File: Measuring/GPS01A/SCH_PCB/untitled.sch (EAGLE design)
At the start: 38 parts, among them SW1 1.55V, T5 BC817, U1 LE33CD-TR, X2 SROUB3M, X3 SROUB3M, X4 SROUB3M, X5 SROUB3M

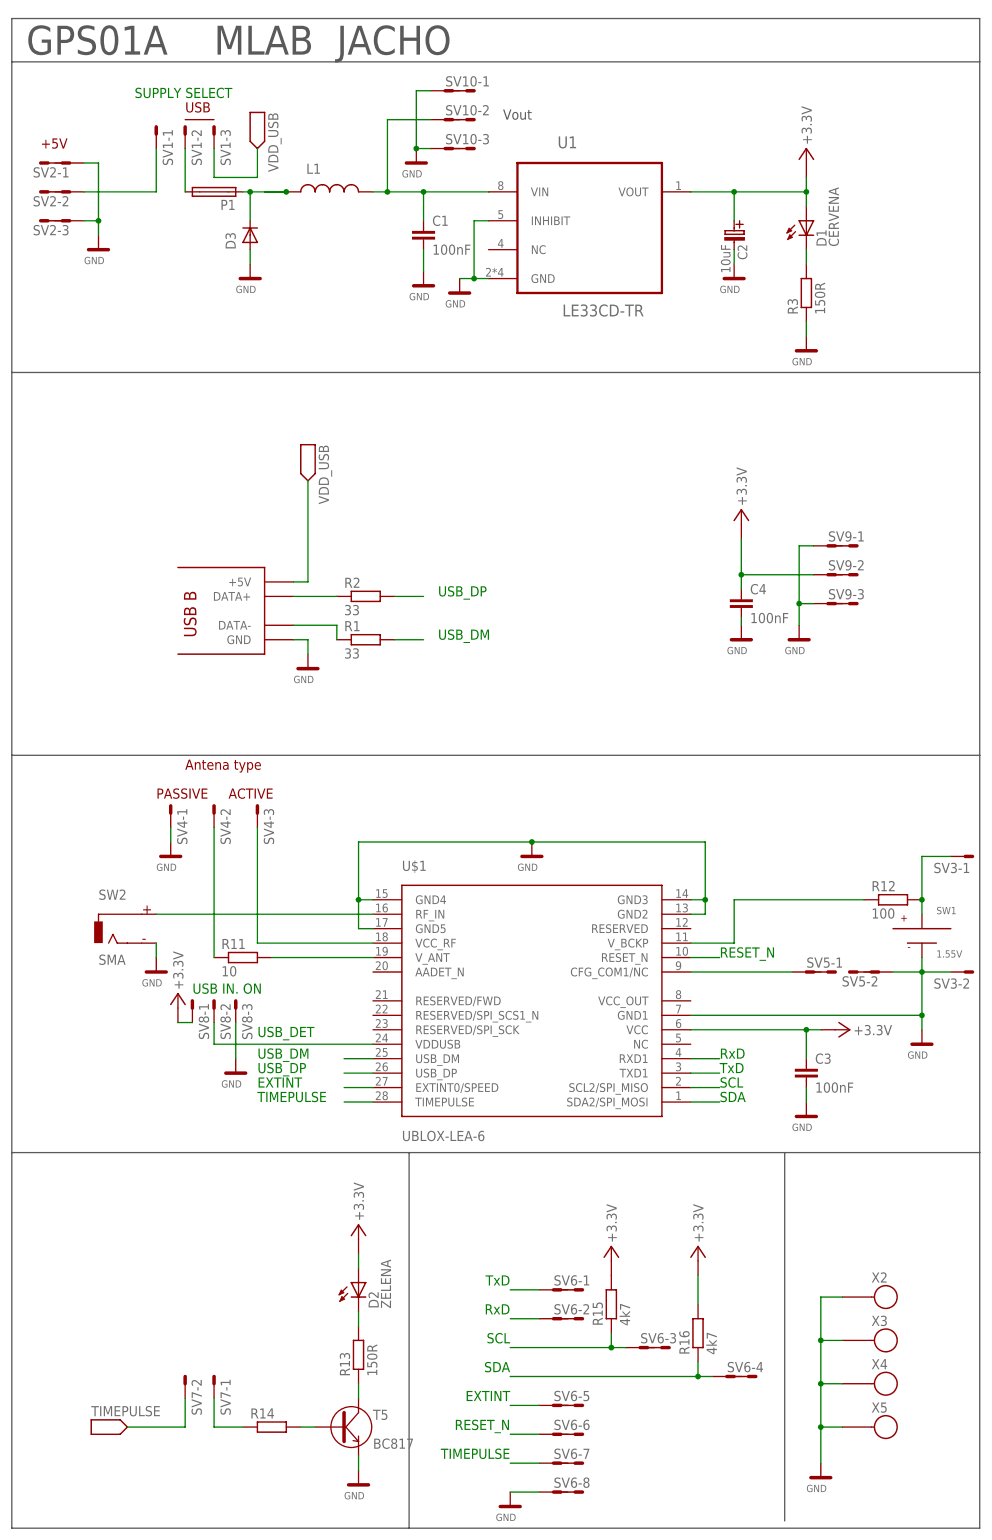
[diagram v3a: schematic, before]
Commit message: 
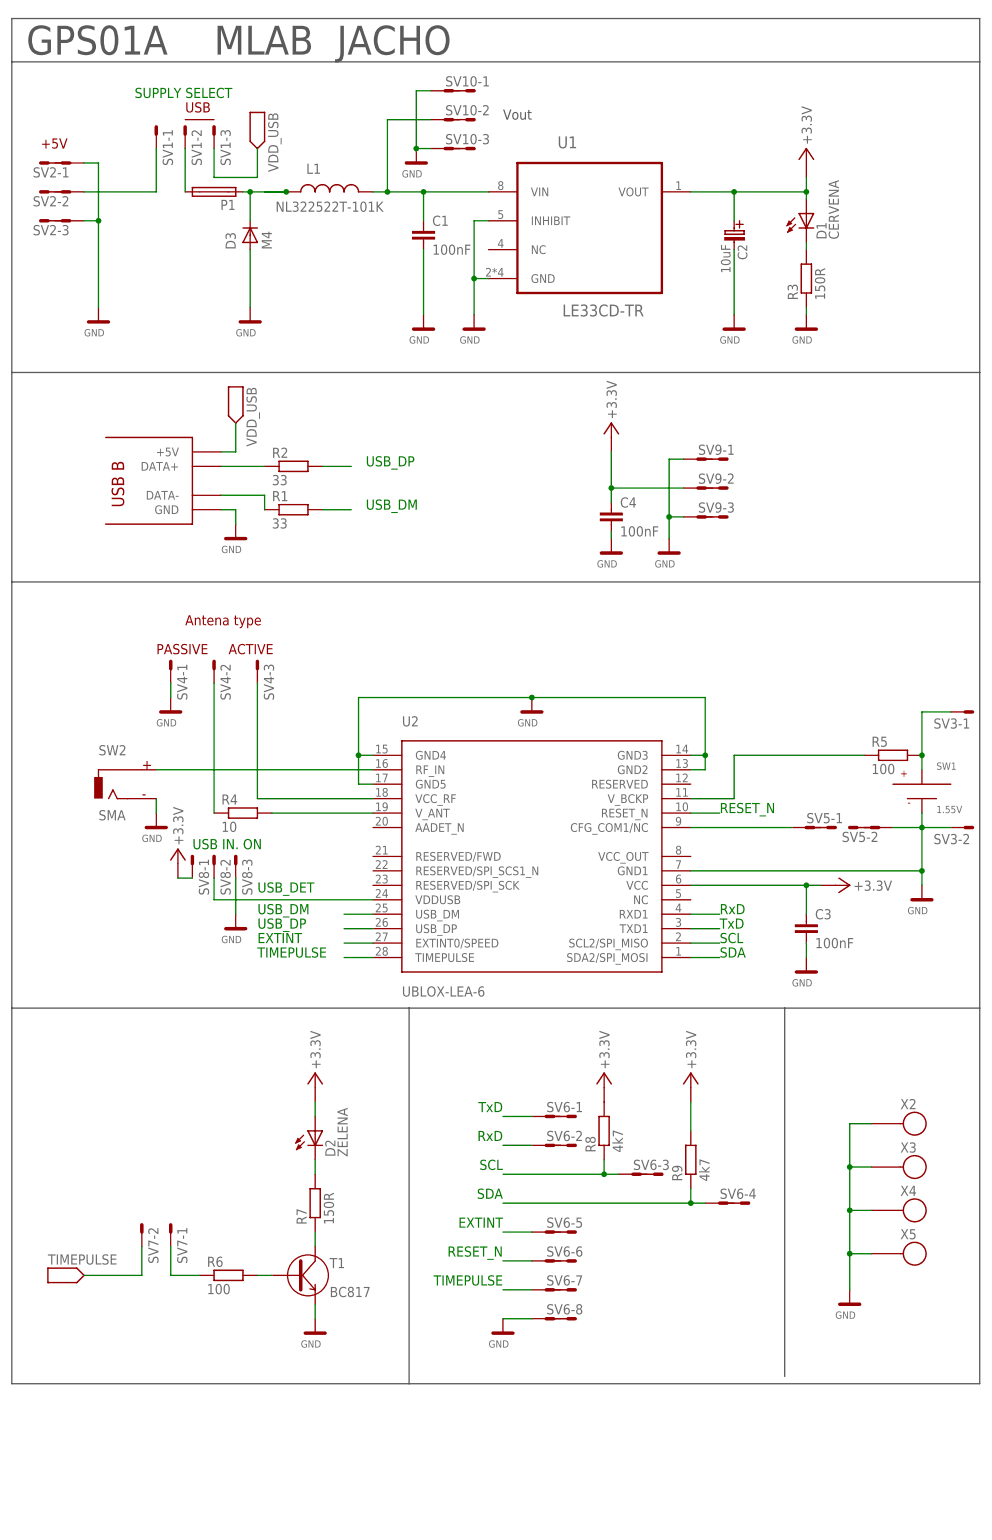
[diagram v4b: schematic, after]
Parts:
- removed R11: 10, moje_R:R0805
- removed R12: 100, moje_R:R0805
- removed R13: 150R, moje_R:R0805
- removed R14: (no value), moje_R:R0805
- removed R15, R16: 4k7, moje_R:R0805
- removed T5: BC817, moje_T:BC817
- removed U$1: UBLOX-LEA-6, 3DRobotics:UBLOX-LEA-6
- added R4: 10, moje_R:R0805
- added R5, R6: 100, moje_R:R0805
- added R7: 150R, moje_R:R0805
- added R8, R9: 4k7, moje_R:R0805
- added T1: BC817, moje_T:BC817
- added U2: UBLOX-LEA-6, 3DRobotics:UBLOX-LEA-6
- D3: value (none) -> M4
- L1: value (none) -> NL322522T-101K
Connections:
- net +3.3V: now also R8.2, R9.2, U2.VCC; no longer R15.2, R16.2, U$1.VCC
- net EXTINT: now also U2.EXTINT0/SPEED; no longer U$1.EXTINT0/SPEED
- net GND: now also T1.E, U2.GND1, U2.GND2, U2.GND3, U2.GND4, U2.GND5; no longer T5.E, U$1.GND1, U$1.GND2, U$1.GND3, U$1.GND4, U$1.GND5
- net N$1: now also U2.RF_IN; no longer U$1.RF_IN
- net N$11: now also R4.2, U2.V_ANT; no longer R11.2, U$1.V_ANT
- net N$13: now also R4.1; no longer R11.1
- net N$14: now also R5.1, U2.V_BCKP; no longer R12.1, U$1.V_BCKP
- net N$15: now also R5.2; no longer R12.2
- net N$16: now also U2.CFG_COM1/NC; no longer U$1.CFG_COM1/NC
- net N$24: now also R7.2; no longer R13.2
- net N$25: now also R7.1, T1.C; no longer R13.1, T5.C
- net N$26: now also R6.2, T1.B; no longer R14.2, T5.B
- net N$27: now also R6.1; no longer R14.1
- net RESET_N: now also U2.RESET_N; no longer U$1.RESET_N
- net RXD: now also U2.RXD1; no longer U$1.RXD1
- net SCL: now also R8.1, U2.SCL2/SPI_MISO; no longer R15.1, U$1.SCL2/SPI_MISO
- net SDA: now also R9.1, U2.SDA2/SPI_MOSI; no longer R16.1, U$1.SDA2/SPI_MOSI
- net TIMEPULSE: now also U2.TIMEPULSE; no longer U$1.TIMEPULSE
- net TXD: now also U2.TXD1; no longer U$1.TXD1
- net USB_DET: now also U2.VDDUSB; no longer U$1.VDDUSB
- net USB_DM: now also U2.USB_DM; no longer U$1.USB_DM
- net USB_DP: now also U2.USB_DP; no longer U$1.USB_DP
- net VCC_RF: now also U2.VCC_RF; no longer U$1.VCC_RF
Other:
- moved on the sheet: C3, C4, D1, D2, R1, R2, R3, SV3-1, SV3-2, SV4-1, SV4-2, SV4-3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

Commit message: 
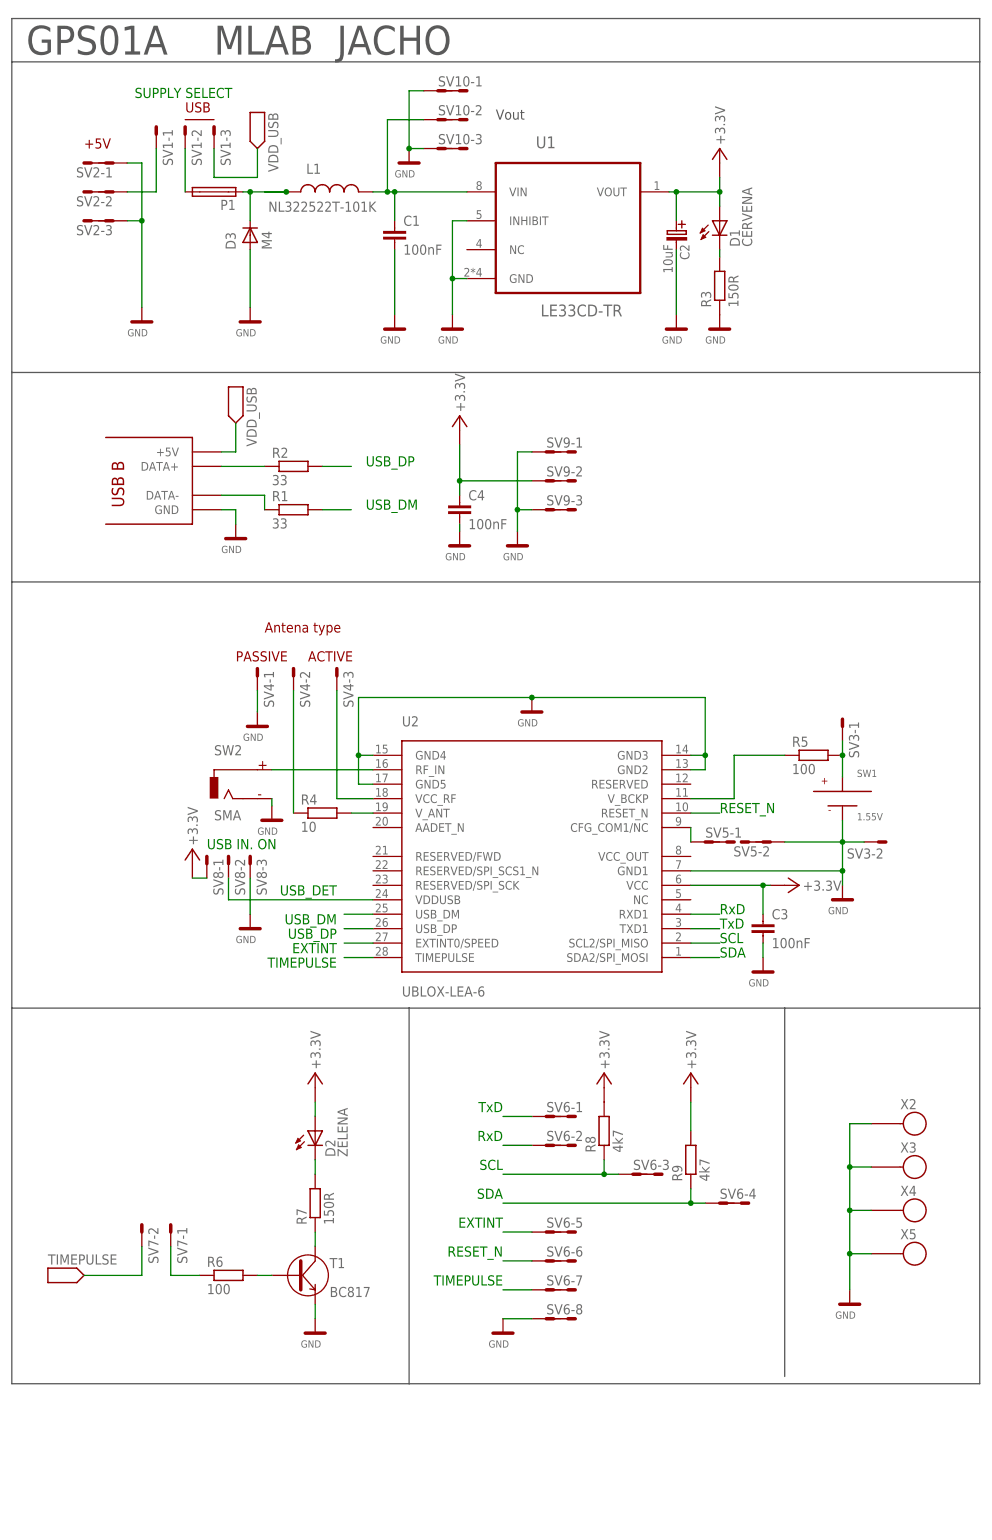
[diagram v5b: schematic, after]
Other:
- moved on the sheet: C1, C2, C3, C4, D1, R3, R4, R5, SV10-1, SV10-2, SV10-3, SV2-1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
